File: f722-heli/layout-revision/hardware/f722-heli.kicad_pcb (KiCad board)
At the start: 6 copper layers, 41.7 x 25.4 mm, 156 parts, among them J1 USB4145-03-0170-C, J10 PORT B / JST GH, J11 PORT C / JST GH, J12 DSM / JST ZH, J2 S1 / GND-VX-S, J3 S2 / GND-VX-S, J4 S3 / GND-VX-S, J5 TAIL / GND-VX-S, J6 ESC / GND-VX-S, J7 RPM / GND-VX-S, J8 SBUS / GND-VX-S, J9 PORT A / JST GH, Q1 BSS138LT1G, Q2 BSS138LT1G, SW1 BOOT / KMT031NGJLHS, U1 STM32F722RET6, U10 TPS2553DRVR / USB input limit, U11 TPS2553DRVR / DSM output limit, U12 USBLC6-4SC6 / header clamp, U13 USBLC6-4SC6 / header clamp, U14 TPD4E05U06DQAR / UART ESD, U15 TPD4E05U06DQAR / UART ESD, U16 PESD15VS2UT,215 / 15V ESD, U2 ICM-42688-P, U3 W25N01GVZEIG / 128MiB, U4 DPS368XTSA1 / 0x76, U5 TPS259472ARPWR, U6 TPS63070RNMR / nominal 5.088V, U7 TPS2117DRLR / ABC priority mux, U8 TPS2121RUXR / BEC-priority co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, U9 TPS62162DSGR / 3.3V 1A, Y1 8MHz / CL10pF / TAXM8M4RDBCCT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

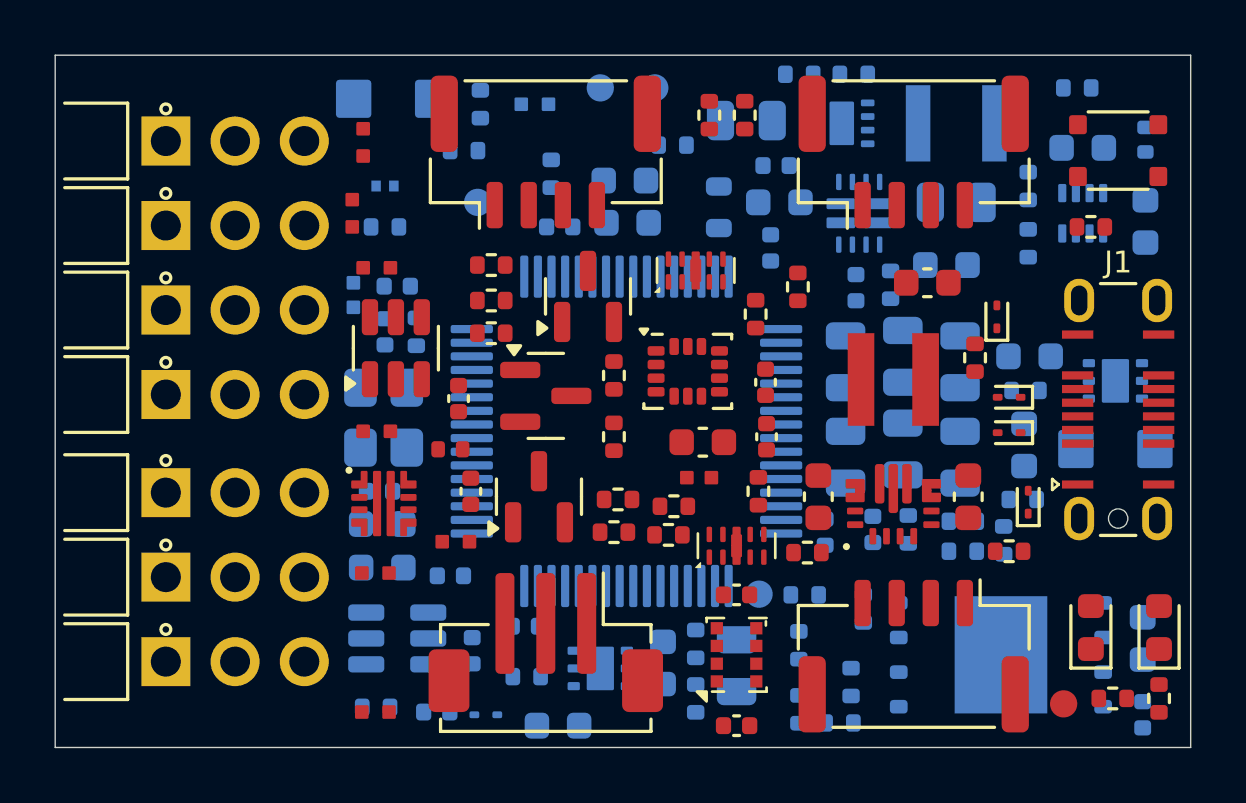
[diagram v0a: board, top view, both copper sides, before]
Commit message: WIP: checkpoint F722 critical routing and ground connectivity
158 unfinished connections; 17 unfinished-interface warnings. Loaded power and ordinary protected signals remain incomplete. Not for manufacture or flight.
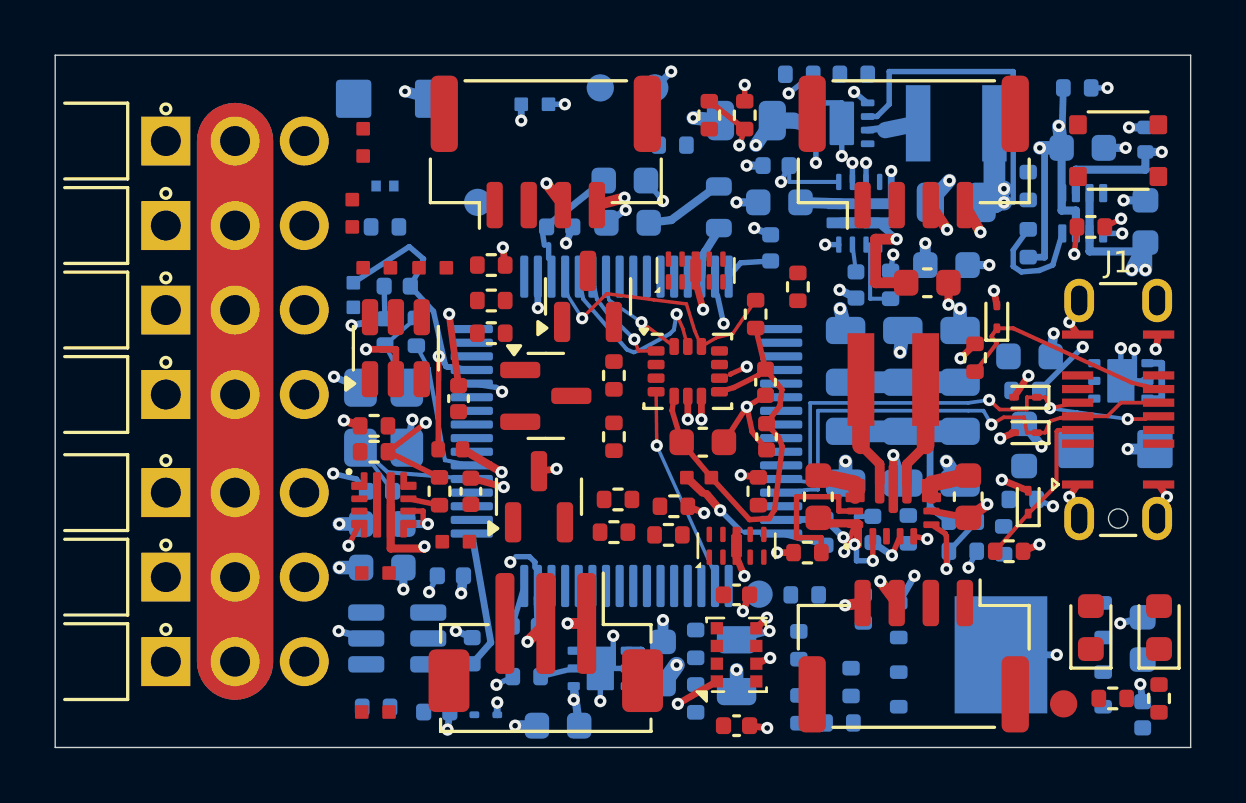
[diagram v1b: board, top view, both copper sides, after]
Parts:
- R50, R51, R52: moved to F.Cu
- moved R52 14.3 mm to (14.1, 16.0)
- moved R51 12.1 mm to (11.7, 14.6), turned to 0 degrees
- moved R50 10.6 mm to (11.7, 13.6)
- moved R23 6.34 mm to (13.8, 7.80)
- moved D3 0.60 mm to (35.6, 13.8)
- moved D4 0.60 mm to (35.6, 12.6)
- moved C56 0.30 mm to (31.1, 14.8)
- moved U10 0.20 mm to (39.1, 11.9)
- moved C53 0.20 mm to (29.0, 11.1)
- moved C71 0.20 mm to (33.2, 11.1)
- moved C62 0.10 mm to (29.4, 8.43)
- moved U5 0.05 mm to (12.1, 16.5)
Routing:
- net GND: track 0.00 -> 119.2 mm, vias 0 -> 109
- net VX_RAW: track 0.00 -> 58.7 mm, vias 0 -> 2
- net +3V3_CORE: track 0.00 -> 40.5 mm, vias 0 -> 4
- net VX_PROTECTED: track 0.00 -> 39.6 mm, vias 0 -> 6
- net +5V_BEC: track 0.00 -> 25.2 mm, vias 0 -> 2
- net USB_N: track 0.00 -> 18.7 mm, vias 0 -> 3
- net USB_P: track 0.00 -> 18.1 mm, vias 0 -> 1
- net +3V3_IMU: track 0.00 -> 15.8 mm
- net USB_LIMITED: track 0.00 -> 14.1 mm, vias 0 -> 2
- net +3V3_ANALOG: track 0.00 -> 13.3 mm, vias 0 -> 1
- net +5V_PERIPH: track 0.00 -> 10.5 mm, vias 0 -> 6
- net IMU_CS: track 0.00 -> 10.3 mm, vias 0 -> 1
- net CORE_BUCK_IN: track 0.00 -> 9.78 mm, vias 0 -> 2
- net CORE_REF: track 0.00 -> 8.65 mm, vias 0 -> 2
- net USB_CC2: track 0.00 -> 8.39 mm
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- added copper zone on In1.Cu, net GND
- added copper zone on In4.Cu, net GND

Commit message: WIP: checkpoint F722 power-input routing at 123 unfinished connections
Zero geometric errors, nine unfinished-interface warnings. CORE, support taps, ordinary routing and loaded qualification remain incomplete. Not for manufacture or flight.
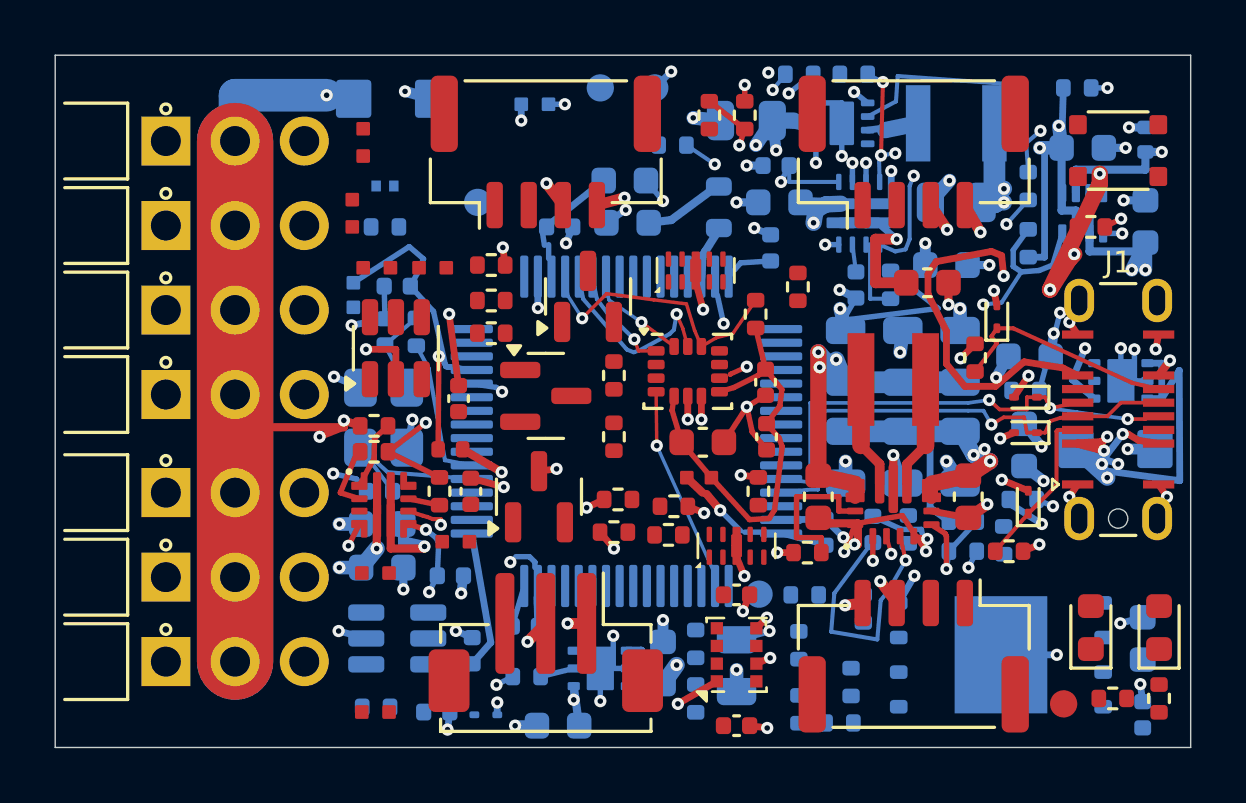
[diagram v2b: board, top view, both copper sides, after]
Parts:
- turned C52 to 180 degrees
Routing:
- net +5V_BEC: track 25.2 -> 141.7 mm, vias 2 -> 6
- net +5V_PERIPH: track 10.5 -> 72.8 mm, vias 6 -> 7
- net USB_VBUS_RAW: track 2.35 -> 55.8 mm, vias 0 -> 10
- net VX_RAW: track 58.7 -> 110.9 mm, vias 2 -> 6
- net USB_LIMITED: track 14.1 -> 50.2 mm, vias 2 -> 7
- net VX_PROTECTED: track 39.6 -> 67.2 mm, vias 6 -> 8
- net CORE_MUX_ST: track 0.00 -> 19.3 mm, vias 0 -> 3
- net CORE_PRIORITY: track 0.00 -> 17.8 mm, vias 0 -> 5
- net CORE_BUCK_IN: track 9.78 -> 25.6 mm, vias 2 -> 3
- net ABC_PG: track 4.30 -> 16.8 mm, vias 0 -> 2
- net GND: track 119.2 -> 129.2 mm, vias 109 -> 110
- net ABC_VAUX: track 1.60 -> 9.55 mm
- net +3V3_CORE: track 40.5 -> 35.9 mm
- net EFUSE_DVDT: track 0.67 -> 3.24 mm, vias 1 -> 2
- net EFUSE_EN: track 0.00 -> 2.56 mm
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
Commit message: WIP: checkpoint F722 routing at 80 unfinished connections
Zero geometric errors and warnings; loaded electrical and signal qualification incomplete. Not ready for fabrication or flight.
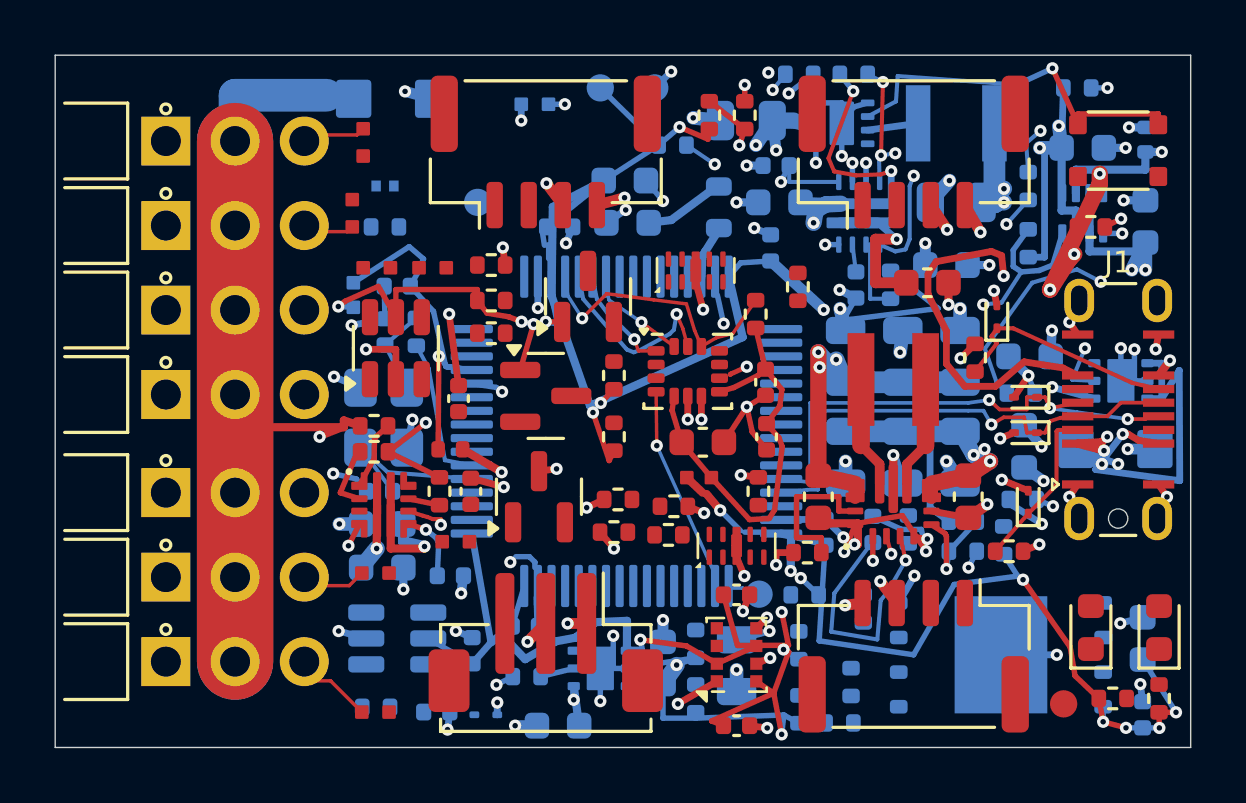
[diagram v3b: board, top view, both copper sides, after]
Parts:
- moved R67 0.20 mm to (35.4, 12.4)
- turned C20 to 180 degrees
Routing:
- net +3V3_CORE: track 35.9 -> 211.5 mm, vias 4 -> 24
- net USB_ILIM: track 0.00 -> 31.9 mm, vias 0 -> 2
- net VX_PROTECTED: track 67.2 -> 75.3 mm, vias 8 -> 9
- net USB_VBUS_RAW: track 55.8 -> 53.1 mm, vias 10 -> 9
- net SBUS_EXT: track 0.00 -> 2.10 mm
- net RPM_EXT: track 0.00 -> 2.09 mm
- net GND: track 129.2 -> 127.7 mm, vias 110 -> 107
- net SERVO1_EXT: track 0.00 -> 1.28 mm
- net CORE_SW: track 3.10 -> 1.87 mm
- net USB_LIMITED: track 50.2 -> 49.1 mm
- net SERVO2_EXT: track 0.00 -> 0.87 mm
- net VX_RAW: track 110.9 -> 110.1 mm, vias 6 -> 3
- net EFUSE_DVDT: track 3.24 -> 2.57 mm, vias 2 -> 1
- net SWCLK: track 0.00 -> 0.61 mm

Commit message: WIP: checkpoint F722 routing at 77 unfinished connections
Zero geometric errors and warnings; loaded electrical and signal qualification incomplete. Not ready for fabrication or flight.
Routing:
- net D1_A: track 0.00 -> 3.14 mm
- net D2_A: track 0.00 -> 3.06 mm
- net SERVO3_EXT: track 0.00 -> 2.72 mm
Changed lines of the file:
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@@
+	)
+	(segment
+		(start 38.32664 20.86402)
+		(end 39.13458 21.67196)
+		(width 0.127)
+		(layer "F.Cu")
+		(net "D1_A")
+	)
+	(segment
+		(start 39.13458 21.67196)
+		(end 39.13458 23.37603)
+		(width 0.127)
+		(layer "F.Cu")
+		(net "D1_A")
+	)
+	(segment
+		(start 38.32664 20.56957)
+		(end 38.32664 20.86402)
+		(width 0.127)
+		(layer "F.Cu")
+		(net "D1_A")
 	)
 	(segment
@@
 	)
 	(segment
+		(start 40.84672 20.55736)
+		(end 40.84672 20.72722)
+		(width 0.127)
+		(layer "F.Cu")
+		(net "D2_A")
+	)
+	(segment
+		(start 40.72397 22.91458)
+		(end 41.19054 22.91458)
+		(width 0.127)
+		(layer "F.Cu")
+		(net "D2_A")
+	)
+	(segment
+		(start 41.19054 21.69227)
+		(end 41.30396 21.57885)
+		(width 0.127)
+		(layer "F.Cu")
+		(net "D2_A")
+	)
+	(segment
+		(start 41.30396 21.18446)
+		(end 41.30396 21.57885)
+		(width 0.127)
+		(layer "F.Cu")
+		(net "D2_A")
+	)
+	(segment
+		(start 40.84672 20.72722)
+		(end 41.30396 21.18446)
+		(width 0.127)
+		(layer "F.Cu")
+		(net "D2_A")
+	)
+	(segment
+		(start 41.19054 21.69227)
+		(end 41.19054 22.91458)
+		(width 0.127)
+		(layer "F.Cu")
+		(net "D2_A")
+	)
+	(segment
+		(start 9.03897 9.24898)
+		(end 10.40558 7.88237)
+		(width 0.127)
+		(layer "F.Cu")
+		(net "SERVO3_EXT")
+	)
+	(segment
+		(start 10.40558 7.88237)
+		(end 11.19591 7.88237)
+		(width 0.127)
+		(layer "F.Cu")
+		(net "SERVO3_EXT")
+	)
+	(segment

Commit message: WIP: checkpoint F722 ADC and flash routing at 75 unfinished connections
Zero geometric errors and warnings; strict paired parity and ERC clean. Loaded electrical and AC qualification incomplete. Not ready for fabrication or flight.
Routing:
- net ADC_DIV_MID: track 0.00 -> 15.2 mm, vias 0 -> 2
- net FLASH_WP_N: track 0.00 -> 9.04 mm, vias 0 -> 2

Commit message: WIP: checkpoint F722 at 69 unfinished connections and confirmed BEC copper deficit
Geometry/ERC clean, but full loaded screen failed. No power correction included. Not ready for fabrication or flight.
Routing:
- net ADC_BEC: track 0.00 -> 13.4 mm, vias 0 -> 1
- net BOOT0: track 0.00 -> 2.89 mm
- net NRST: track 0.00 -> 2.49 mm, vias 0 -> 1
- net ADC_BUS: track 0.00 -> 1.02 mm
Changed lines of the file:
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@@
 	)
 	(segment
+		(start 18.2093 16.40802)
+		(end 19.25569 15.36163)
+		(width 0.127)
+		(layer "F.Cu")
+		(net "ADC_BEC")
+	)
+	(segment
+		(start 19.25569 15.36163)
+		(end 20.28986 15.36163)
+		(width 0.127)
+		(layer "F.Cu")
+		(net "ADC_BEC")
+	)
+	(segment
+		(start 17.08861 18.06907)
+		(end 18.2093 16.94838)
+		(width 0.127)
+		(layer "F.Cu")
+		(net "ADC_BEC")
+	)
+	(segment
+		(start 15.47545 16.67264)
+		(end 15.47545 17.03901)
+		(width 0.127)
+		(layer "F.Cu")
+		(net "ADC_BEC")
+	)
+	(segment
+		(start 21.36646 16.32603)
+		(end 22.01458 16.32603)
+		(width 0.127)
+		(layer "F.Cu")
+		(net "ADC_BEC")
+	)
+	(segment
+		(start 16.50551 18.06907)
+		(end 17.08861 18.06907)
+		(width 0.127)
+		(layer "F.Cu")
+		(net "ADC_BEC")
+	)
+	(segment
+		(start 15.47545 17.03901)
+		(end 16.50551 18.06907)
+		(width 0.127)
+		(layer "F.Cu")
+		(net "ADC_BEC")
+	)
+	(segment
+		(start 18.2093 16.40802)
+		(end 18.2093 16.94838)
+		(width 0.127)
+		(layer "F.Cu")
+		(net "ADC_BEC")
+	)
+	(segment
+		(start 20.28986 15.36163)
+		(end 20.98442 16.05619)
+		(width 0.127)
+		(layer "F.Cu")
+		(net "ADC_BEC")
+	)
+	(via
+		(at 19.93661 15.36163)
+		(size 0.45)
+		(drill 0.2)
+		(layers "F.Cu" "B.Cu")
+		(tenting
+			(front yes)
+			(back yes)
+		)
+		(net "ADC_BEC")
+	)
+	(segment
+		(start 15.98485 13.55052)
+		(end 18.1255 13.55052)
+		(width 0.127)
+		(layer "B.Cu")
+		(net "ADC_BEC")
+	)
+	(segment
+		(start 18.1255 13.55052)
+		(end 19.93661 15.36163)
+		(width 0.127)
+		(layer "B.Cu")
+		(net "ADC_BEC")
+	)
+	(segment
 		(start 15.49 8.6)
 		(end 12.5 8.6)
@@
 	)
 	(segment
+		(start 21.89 17.5)
+		(end 21.99 17.6)
+		(width 0.127)
+		(layer "F.Cu")
+		(net "ADC_BUS")
+	)
+	(segment
+		(start 21.01 17.5)
+		(end 21.89 17.5)
+		(width 0.127)
+		(layer "F.Cu")
+		(net "ADC_BUS")
+	)
+	(segment
 		(start 9.36475 22.95646)
 		(end 10.10646 22.95646)
@@
 	)
 	(segment
+		(start 15.01263 13.26349)
+		(end 16.07081 14.32167)
+		(width 0.127)
+		(layer "F.Cu")
+		(net "NRST")
+	)
+	(segment
+		(start 16.07081 14.32167)
+		(end 16.47327 14.32167)
+		(width 0.127)
+		(layer "F.Cu")
+		(net "NRST")
+	)
+	(via
+		(at 16.47327 14.32167)
+		(size 0.45)
+		(drill 0.2)
+		(layers "F.Cu" "B.Cu")
+		(tenting
+			(front yes)
+			(back yes)
+		)
+		(net "NRST")
+	)
+	(segment
+		(start 16.41974 14.32167)
+		(end 16.47327 14.32167)
+		(width 0.127)
+		(layer "B.Cu")
+		(net "NRST")
+	)
+	(segment
+		(start 16.32187 14.47307)
+		(end 16.47327 14.32167)
+		(width 0.127)
+		(layer "B.Cu")
+		(net "NRST")
+	)
+	(segment
+		(start 15.99629 14.47307)
+		(end 16.32187 14.47307)
+		(width 0.127)
+		(layer "B.Cu")
+		(net "NRST")
+	)
+	(segment
 		(start 39.35 13.35)
 		(end 40 13.35)
@@
 	)
 	(segment
+		(start 37.76486 4.18823)
+		(end 38.09466 3.85843)
+		(width 0.127)
+		(layer "F.Cu")
+		(net "BOOT0")
+	)
+	(segment
+		(start 39.90843 3.85843)
+		(end 40.34054 4.29054)
+		(width 0.127)
+		(layer "F.Cu")
+		(net "BOOT0")
+	)
+	(segment
+		(start 38.09466 3.85843)
+		(end 39.90843 3.85843)
+		(width 0.127)
+		(layer "F.Cu")
+		(net "BOOT0")
+	)
+	(segment

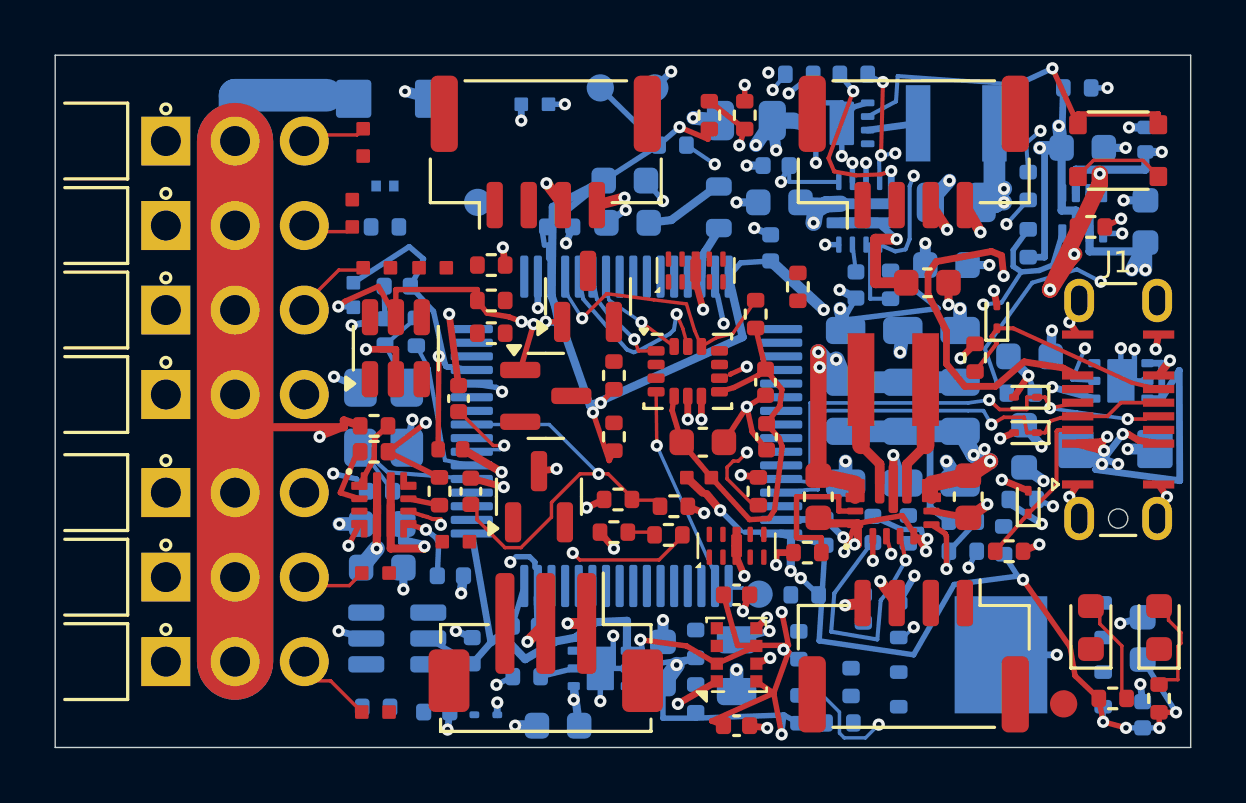
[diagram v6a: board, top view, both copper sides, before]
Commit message: WIP: checkpoint F722 corrected power routing at 62 unfinished connections
Conditional power screens pass within declared scope; overloaded illustration remains failed. Not ready for fabrication or flight.
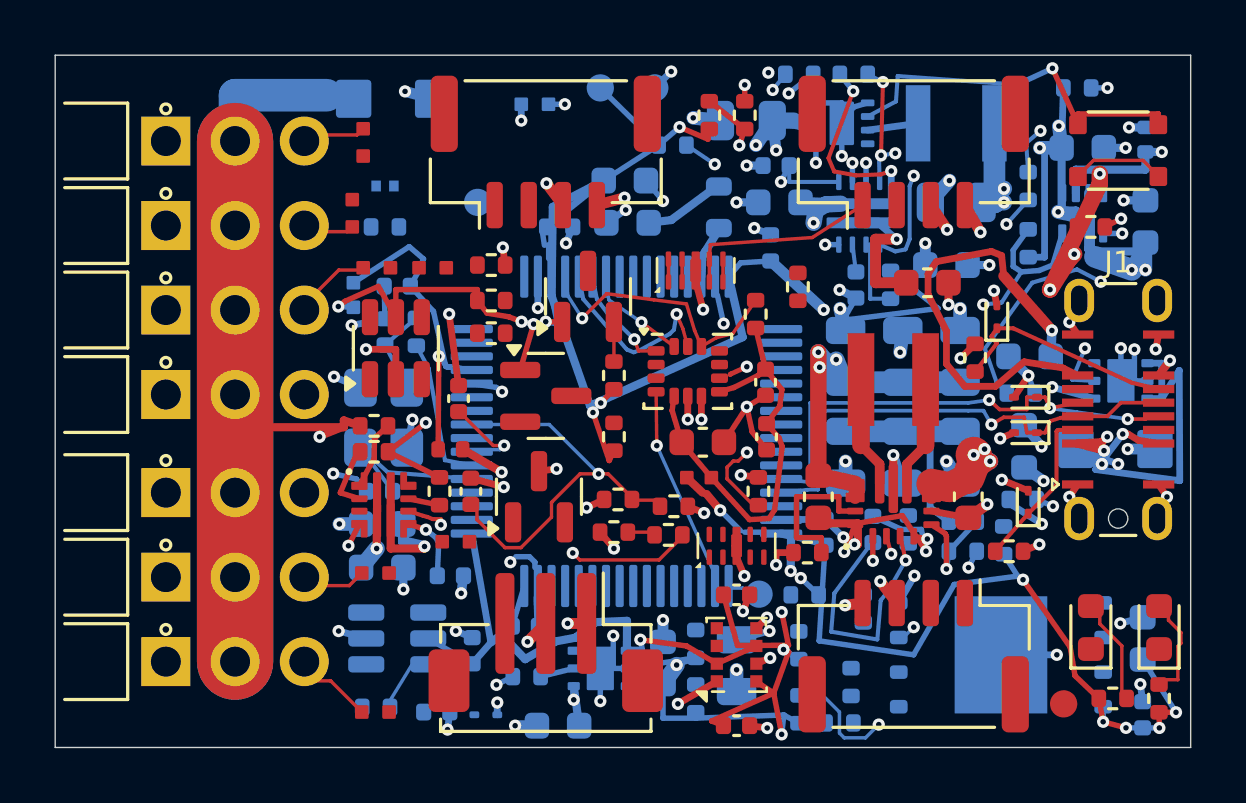
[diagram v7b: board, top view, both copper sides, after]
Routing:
- net +5V_BEC: track 141.7 -> 155.3 mm, vias 6 -> 7
- net PORT_B_RX_EXT: track 0.00 -> 7.31 mm
- net +5V_PERIPH: track 72.8 -> 75.4 mm
- net RPM_MCU: track 0.00 -> 1.56 mm
- net USB_VBUS_RAW: track 53.1 -> 52.2 mm, vias 9 -> 8
- net PORT_B_TX_EXT: track 0.00 -> 0.84 mm
- net PORT_A_TX_EXT: track 0.00 -> 0.84 mm
- net PORT_A_RX_EXT: track 0.00 -> 0.84 mm
- net SBUS_LV: track 0.00 -> 0.60 mm
